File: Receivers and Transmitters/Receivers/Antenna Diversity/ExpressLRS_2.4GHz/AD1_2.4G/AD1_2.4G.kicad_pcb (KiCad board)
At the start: 4 copper layers, 39.5 x 39.5 mm, 52 parts, among them J1 Conn_01x04_Socket, J3 Conn_01x04_Pin, U1 TPS7A4701xRGW, U2 SX1280IMLTRT, U3 ESP8285H16, U4 SE2431L-R, Y1 52MHz, Y2 26MHz

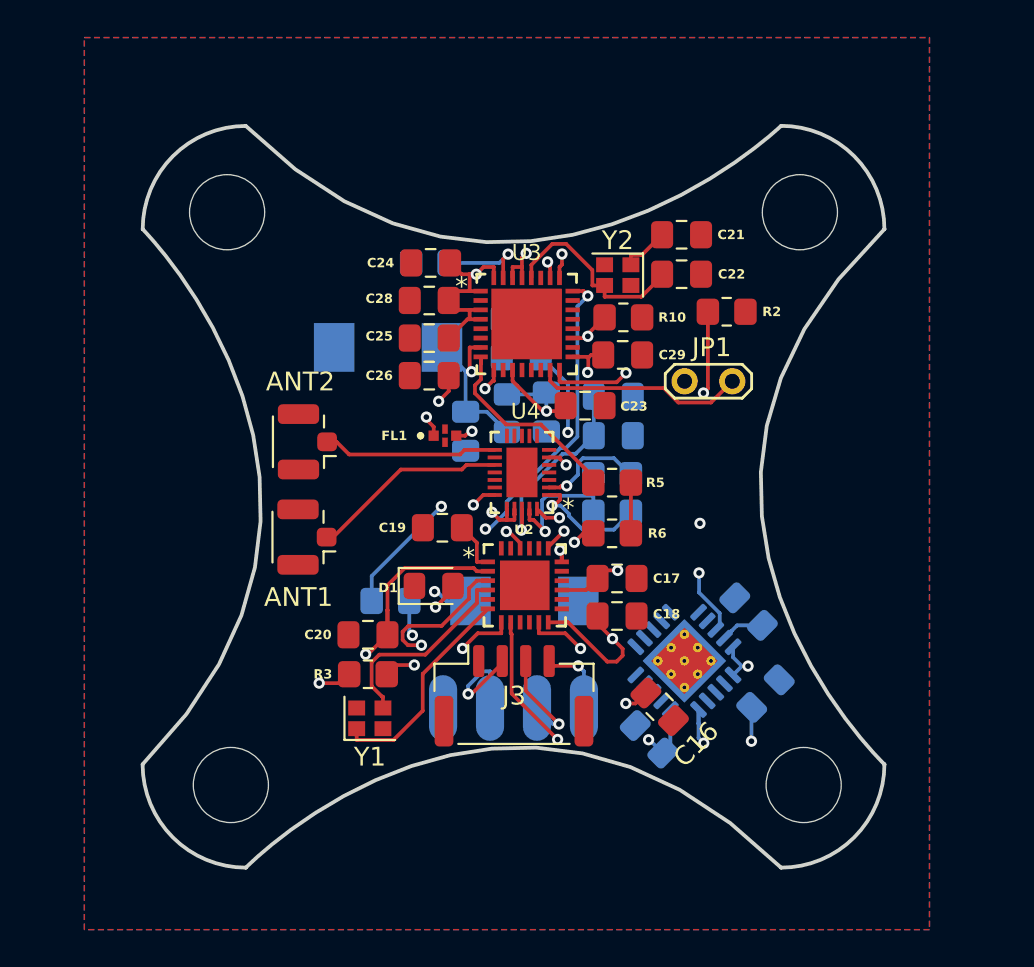
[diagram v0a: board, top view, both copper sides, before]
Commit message: Update Antenna Diversity (AD1_2.4G), True Antenna Diversity (TD1_2.4G), and Gemini Mode transmitter (G_TX1): Modify KiCad files, add BOMs and production files; update images, docs, videos, and README; remove outdated Mechanical CAD file
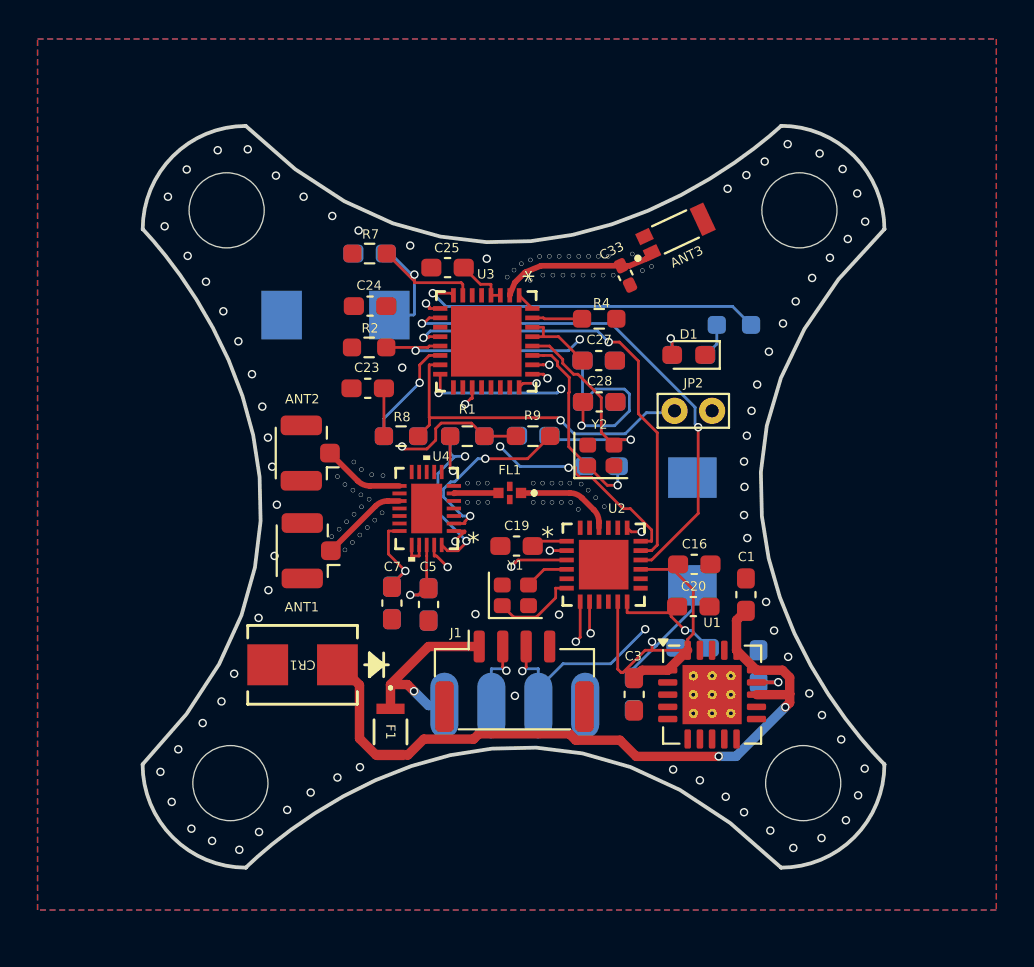
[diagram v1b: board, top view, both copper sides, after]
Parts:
- removed G***: LOGO, logo:logo
- removed J3: Conn_01x04_Pin, Connector_JST:JST_GH_SM04B-GHS-TB_1x04-1MP_P1.25mm_Horizontal
- removed JP1: Jumper_2_Bridged, TestPoint:TestPoint_2Pads_Pitch2.54mm_Drill0.8mm
- added ANT3: W3008, W3008:ANTENNA_W3008, F.Cu at (147.2, 77.7)
- added C33: 1.5pF, Capacitor_SMD:C_0402_1005Metric_Pad0.74x0.62mm_HandSolder, F.Cu at (144.5, 80.0)
- added CR1: SMBJ60A, ul_SMBJ60A:SMBJSeries_LTF, F.Cu at (127.3, 100.7)
- added F1: MF-PSMF020X-2, ul_MF-PSMF020X-2:FUSE_F020X_BRN, F.Cu at (132.0, 104.3)
- added J2: Conn_01x04_Socket, Connector_Harwin:Harwin_M20-89004xx_1x04_P2.54mm_Horizontal, B.Cu at (138.2, 105.3)
- added JP2: Jumper_2_Small_Bridged, TestPoint:TestPoint_Bridge_Pitch2.0mm_Drill0.7mm, F.Cu at (147.1, 87.2)
- C1, C27, C3, C5, C7: footprint Capacitor_SMD:C_0805_2012Metric_Pad1.18x1.45mm_HandSolder -> Capacitor_SMD:C_0603_1608Metric_Pad1.08x0.95mm_HandSolder; moved to F.Cu
- C16, C19, C2, C20, C23, C24, C25, C28, C31, C4, C6: footprint Capacitor_SMD:C_0805_2012Metric_Pad1.18x1.45mm_HandSolder -> Capacitor_SMD:C_0603_1608Metric_Pad1.08x0.95mm_HandSolder
- C17, C18, C21, C22, C26, C29: footprint Capacitor_SMD:C_0805_2012Metric_Pad1.18x1.45mm_HandSolder -> Capacitor_SMD:C_0603_1608Metric_Pad1.08x0.95mm_HandSolder; moved to B.Cu
- D1: footprint LED_SMD:LED_0805_2012Metric_Pad1.15x1.40mm_HandSolder -> LED_SMD:LED_0603_1608Metric_Pad1.05x0.95mm_HandSolder
- J1: value Conn_01x04_Socket -> Conn_01x04_Pin; footprint Connector_Harwin:Harwin_M20-89004xx_1x04_P2.54mm_Horizontal -> Connector_JST:JST_GH_SM04B-GHS-TB_1x04-1MP_P1.25mm_Horizontal; moved to F.Cu
- R1, R4, R7, R8, R9: footprint Resistor_SMD:R_0805_2012Metric_Pad1.20x1.40mm_HandSolder -> Resistor_SMD:R_0603_1608Metric_Pad0.98x0.95mm_HandSolder; moved to F.Cu
- R10, R3, R5, R6: footprint Resistor_SMD:R_0805_2012Metric_Pad1.20x1.40mm_HandSolder -> Resistor_SMD:R_0603_1608Metric_Pad0.98x0.95mm_HandSolder; moved to B.Cu
- R2: footprint Resistor_SMD:R_0805_2012Metric_Pad1.20x1.40mm_HandSolder -> Resistor_SMD:R_0603_1608Metric_Pad0.98x0.95mm_HandSolder
- U1: moved to F.Cu
- moved R2 19.1 mm to (130.9, 83.8), turned to 0 degrees
- moved D1 18.3 mm to (147.9, 84.2), turned to 180 degrees
- moved C20 17.4 mm to (148.1, 97.6), turned to 0 degrees
- moved C7 16.6 mm to (132.1, 97.4), turned to -90 degrees
- moved C4 14.8 mm to (134.0, 97.5), turned to -90 degrees
- moved C6 14.8 mm to (132.1, 97.4), turned to -90 degrees
- moved C5 13.3 mm to (134.0, 97.5), turned to -90 degrees
- moved C21 13.0 mm to (143.2, 90.1), turned to 180 degrees
- moved R3 12.8 mm to (132.6, 88.5), turned to 180 degrees
- moved C22 11.7 mm to (139.6, 88.5), turned to 180 degrees
- moved C23 11.6 mm to (130.8, 86.0), turned to 180 degrees
- moved R7 11.2 mm to (130.9, 78.8), turned to 0 degrees
- moved C31 10.8 mm to (130.9, 78.8), turned to 0 degrees
- moved R5 10.6 mm to (150.3, 82.6), turned to 180 degrees
- moved C28 10.5 mm to (143.1, 86.7), turned to 0 degrees
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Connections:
- C1 pad 1: +5V -> F2
- J1 pad 1: GND -> +5V
- J1 pad 2: +5V -> /TX
- J1 pad 3: /TX -> /RX
- J1 pad 4: /RX -> GND
- U1 pad 13: +5V -> F2
- U1 pad 15: +5V -> F2
- U1 pad 16: +5V -> F2
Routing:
- net F2: track 0.00 -> 38.8 mm, vias 0 -> 2
- net /SE2431L/TR: track 30.8 -> 2.39 mm, vias 2 -> 0
- net /ESP8285/SX_MISO: track 0.00 -> 27.3 mm, vias 0 -> 2
- net /ESP8285/SX_MOSI: track 0.00 -> 24.4 mm, vias 0 -> 2
- net Net-(JP2-A): track 36.1 -> 18.6 mm
- net /SX1280/VDD_INN: track 33.3 -> 19.4 mm
- net /TX: track 35.2 -> 23.0 mm
- net /ESP8285/SX_NRESET: track 10.4 -> 22.1 mm
- net /SE2431L/VCC2: track 15.5 -> 5.36 mm, vias 2 -> 1
- net Net-(D1-A): track 11.6 -> 1.80 mm, vias 2 -> 1
- net Net-(U3-LNA): track 0.00 -> 8.54 mm
- net Net-(U2-XTA): track 10.9 -> 2.38 mm
- net Net-(U3-XTAL_OUT): track 2.63 -> 10.8 mm, vias 0 -> 1
- net /ESP8285/DIO1: track 32.7 -> 24.6 mm, vias 2 -> 3
- net /ESP8285/LED: track 10.9 -> 18.8 mm, vias 0 -> 1
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- added copper zone on In2.Cu, net +3.3V
- added copper zone on In1.Cu, net GND
- added copper zone on In3.Cu, net GND
- added copper zone on In4.Cu, net GND
- removed copper zone on In1.Cu, net +3.3V
- removed copper zone on In2.Cu, net +5V
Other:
- copper layers 4 -> 6
